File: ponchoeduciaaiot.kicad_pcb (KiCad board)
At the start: 2 copper layers, 41 parts, among them J1 TB_1X3, J2 TB_1X2, J3 TB_1X2, Q1 BC548, Q2 BC548, U1 4N25, U2 LM35, U3 4N25, U4 RELAY, U5 RELAY, U6 RN1810E

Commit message: placing de componentes
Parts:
- moved D8 224.7 mm to (38.8, 35.0), turned to 90 degrees
- moved C6 218.9 mm to (54.0, 31.0), turned to 90 degrees
- moved C2 215.9 mm to (52.0, 51.2), turned to 90 degrees
- moved C1 209.0 mm to (60.0, 32.5), turned to 90 degrees
- moved R15 206.5 mm to (38.8, 28.8)
- moved C4 197.5 mm to (58.0, 52.8), turned to 90 degrees
- moved R13 195.1 mm to (63.0, 60.0), turned to 90 degrees
- moved R12 177.6 mm to (68.0, 60.0), turned to 90 degrees
- moved R14 172.5 mm to (73.2, 52.8)
- moved C5 170.9 mm to (90.8, 32.2), turned to 90 degrees
- moved C3 159.8 mm to (96.8, 30.8), turned to 90 degrees
- moved U6 158.9 mm to (66.2, 47.0)
- moved U2 155.1 mm to (116.0, 33.5), turned to 90 degrees
- moved R7 118.2 mm to (109.8, 38.8), turned to 90 degrees
- moved D3 113.3 mm to (106.5, 44.0)
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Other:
- board outline added: 86.5 x 96.5 mm

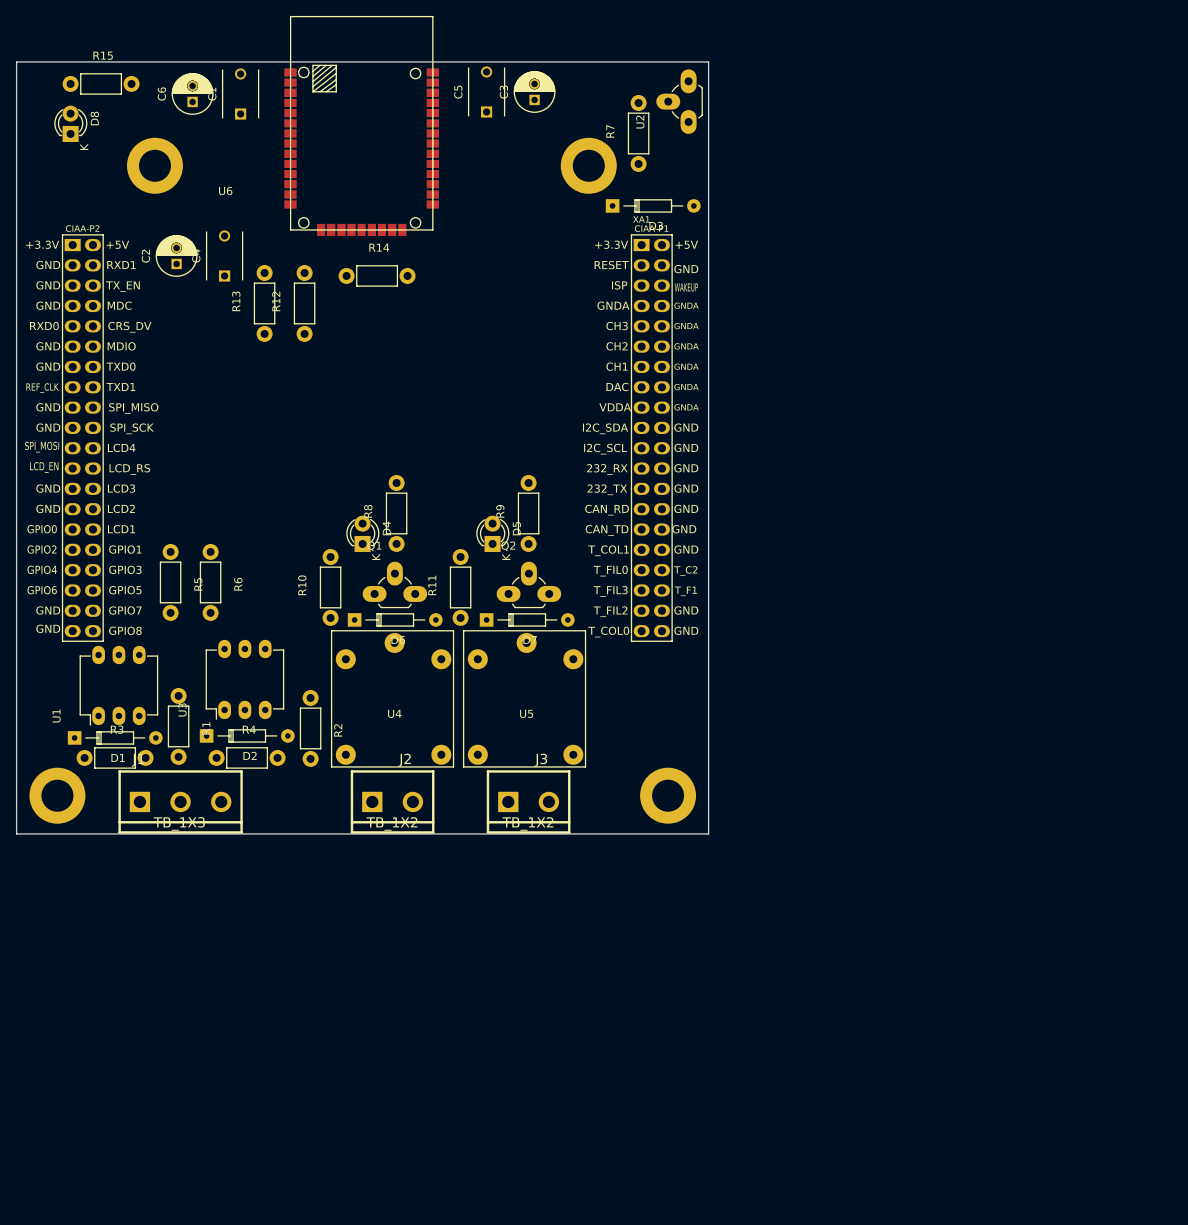
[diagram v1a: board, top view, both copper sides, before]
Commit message: correcciones en esquemarico. ERC OK. Se crearon rotulos. PCB: replacing mas compacto
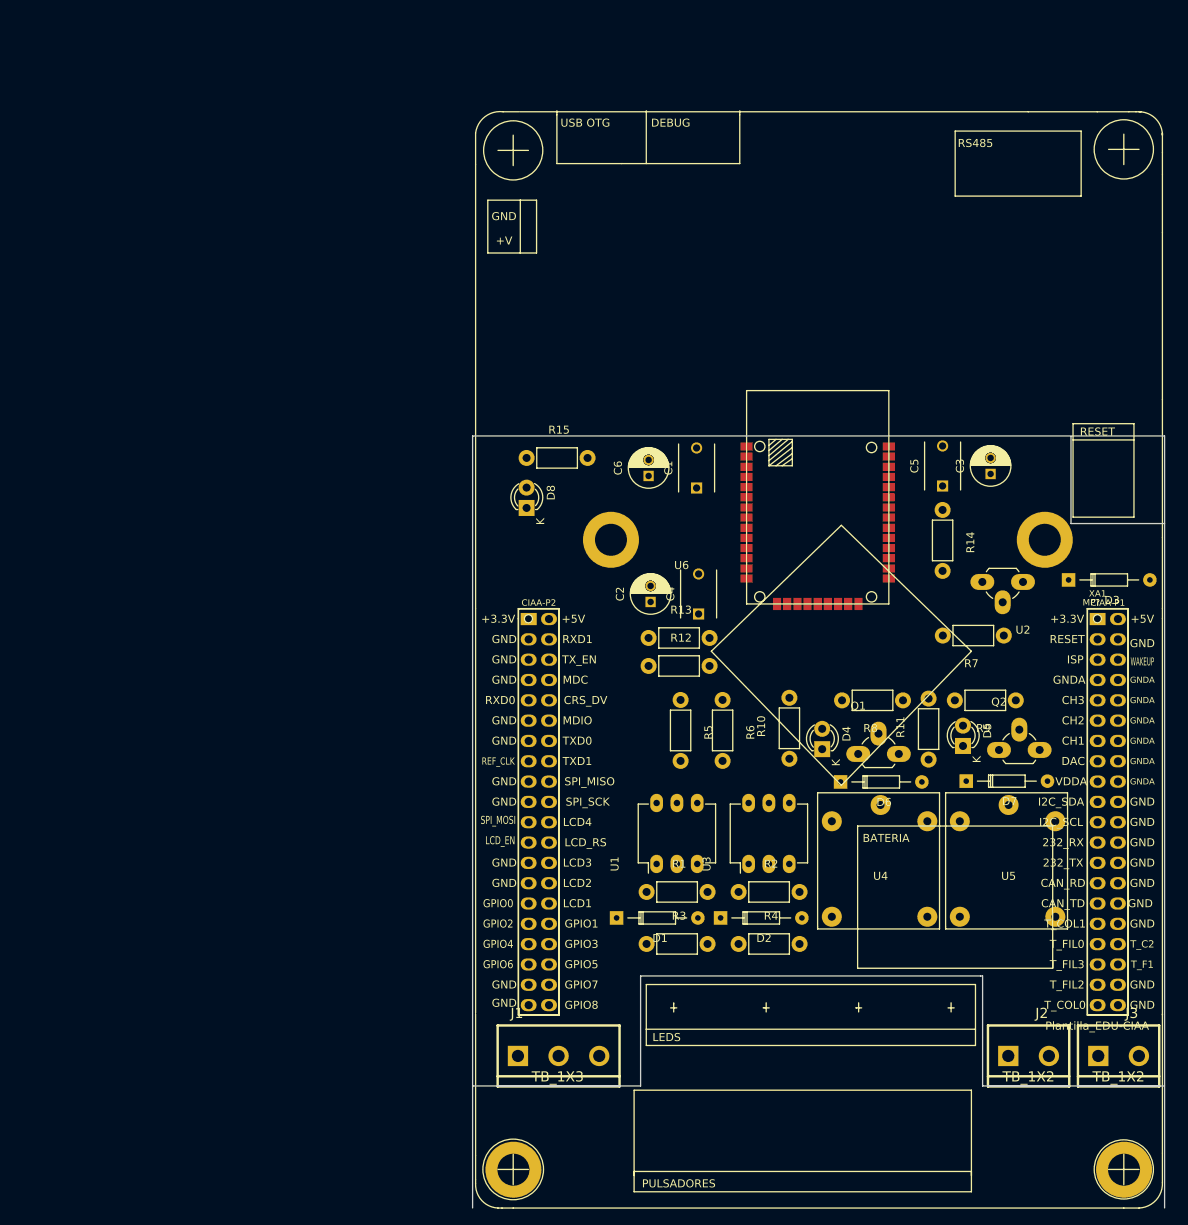
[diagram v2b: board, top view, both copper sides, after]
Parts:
- added MP?: Plantilla_EDU-CIAA, ponchoeduciaaiot:Plantilla_EDU-CIAA, F.Cu at (167.1, 95.6)
- moved J2 85.6 mm to (158.5, 150.2)
- moved J3 80.3 mm to (169.8, 150.2)
- moved R14 80.0 mm to (147.8, 82.0), turned to 270 degrees
- moved R7 74.6 mm to (155.4, 97.7), turned to 180 degrees
- moved R3 74.0 mm to (110.8, 136.2)
- moved C1 73.7 mm to (117.0, 79.2)
- moved C3 73.7 mm to (153.8, 77.5)
- moved C5 73.7 mm to (147.8, 79.0)
- moved C6 73.7 mm to (111.0, 77.8)
- moved D3 73.7 mm to (163.5, 90.8)
- moved D8 73.7 mm to (95.8, 81.8)
- moved R15 73.7 mm to (95.8, 75.5)
- moved U6 73.7 mm to (123.2, 93.8)
- moved XA1 73.7 mm to (167.1, 95.6)
- moved C2 72.8 mm to (111.2, 93.5)
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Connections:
- D2 pad 2: Net-(D2-Pad2) -> Net-(D1-Pad2)
- R4 pad 2: Net-(D2-Pad2) -> Net-(D1-Pad2)
- U3 pad 2: Net-(D2-Pad2) -> Net-(D1-Pad2)
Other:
- outline, holes or cut-outs redrawn
- board text added: "Extra information:"
- board text added: "Grid: 0.2500mm Track with:1mm Via:0.6mm / 0.4mm Layers: 2 PCB Surface Finishes: HASL"

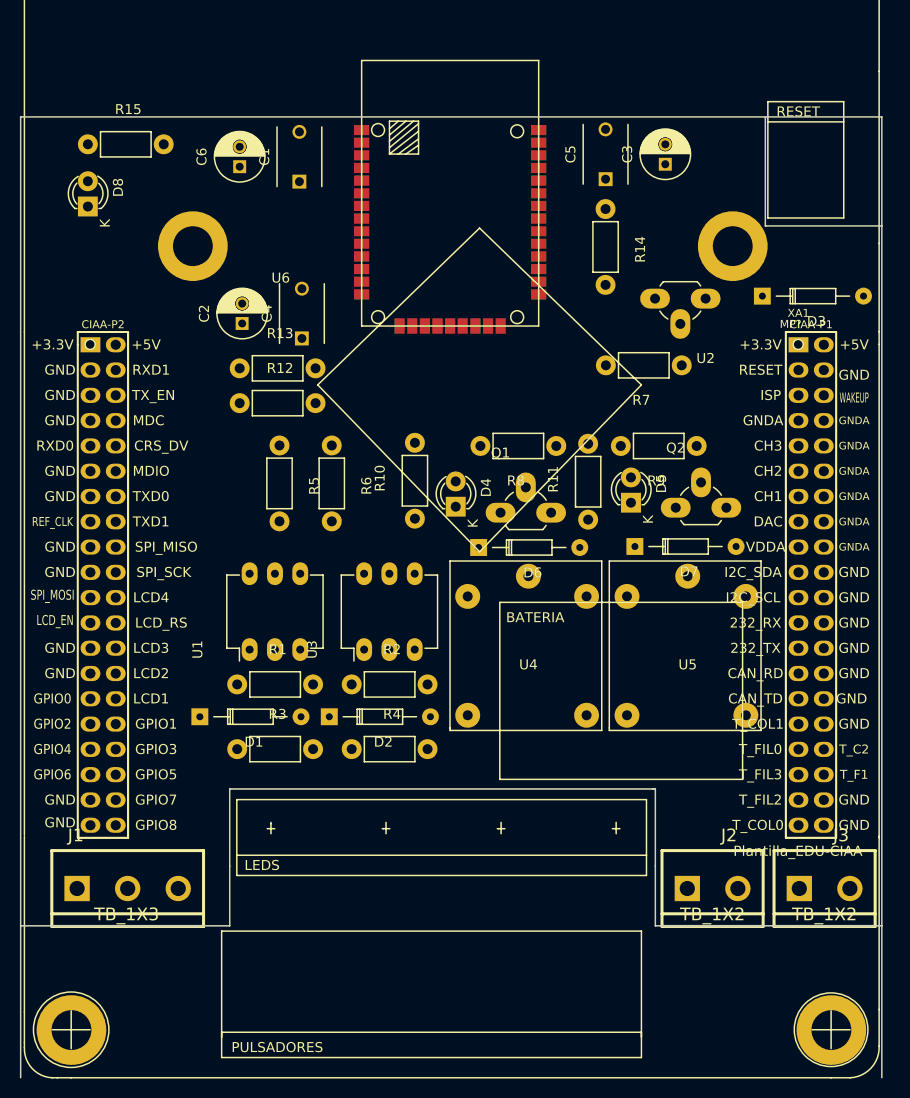
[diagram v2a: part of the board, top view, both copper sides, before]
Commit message: comienzo ruteo
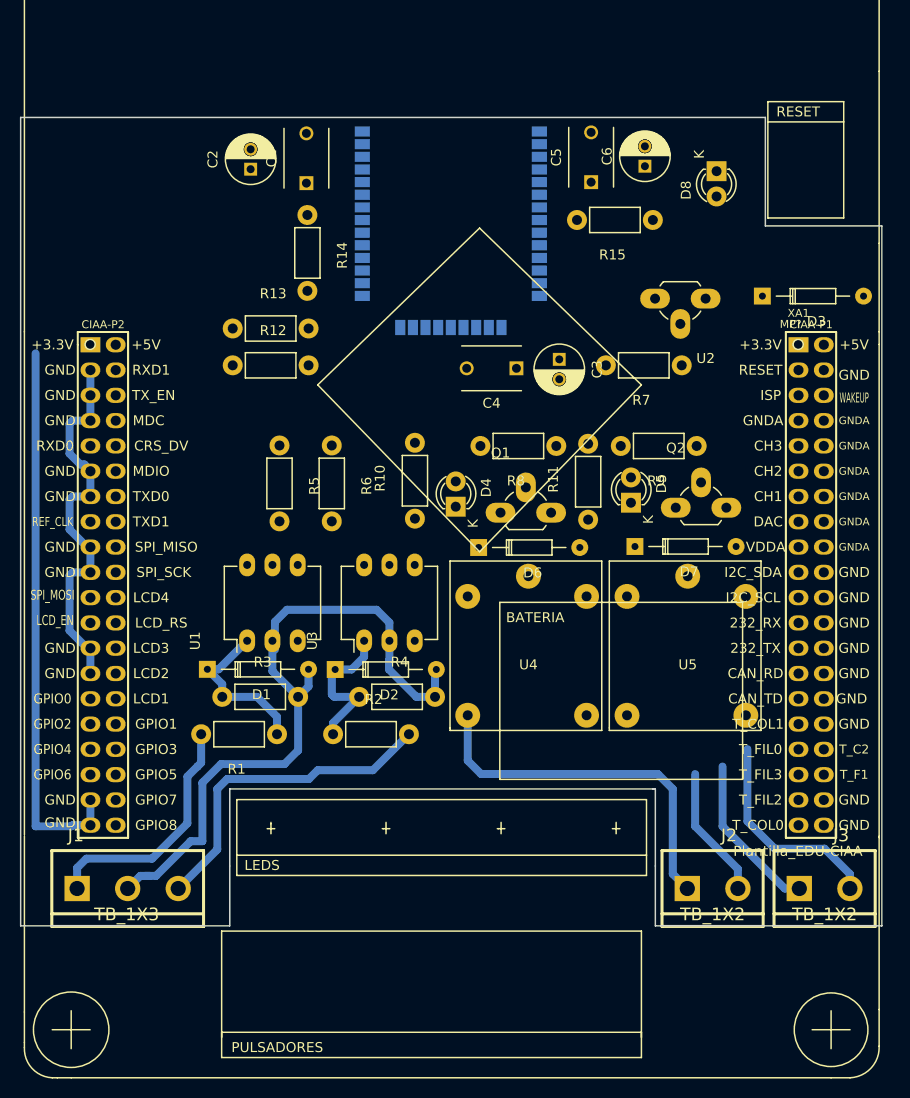
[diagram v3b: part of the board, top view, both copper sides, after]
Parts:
- U6: moved to B.Cu
- moved D8 63.2 mm to (158.9, 78.2), turned to 270 degrees
- moved R15 57.3 mm to (152.5, 83.1), turned to 180 degrees
- moved C6 40.7 mm to (151.7, 77.7)
- moved R14 30.0 mm to (117.8, 82.6)
- moved C3 22.3 mm to (143.1, 97.1), turned to 270 degrees
- moved C4 21.8 mm to (138.8, 98.0), turned to 180 degrees
- moved U6 17.9 mm to (141.1, 93.9), turned to 180 degrees
- moved C2 15.5 mm to (112.1, 78.0)
- moved R1 6.40 mm to (114.8, 134.8), turned to 180 degrees
- moved R3 5.46 mm to (109.2, 131.0)
- moved R2 5.34 mm to (120.4, 134.8)
- moved R4 5.30 mm to (123.0, 131.0)
- moved D1 4.82 mm to (107.8, 128.2)
- moved D2 4.78 mm to (120.6, 128.3)
- moved R13 4.06 mm to (110.3, 94.0)
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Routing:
- net GND: track 0.00 -> 95.1 mm
- net Net-(D1-Pad2): track 0.00 -> 71.6 mm
- net Net-(J2-Pad1): track 0.00 -> 36.9 mm
- net Net-(J1-Pad3): track 0.00 -> 33.2 mm
- net Net-(J1-Pad1): track 0.00 -> 24.5 mm
- net Net-(J3-Pad2): track 0.00 -> 21.2 mm
- net Net-(D1-Pad1): track 0.00 -> 16.6 mm
- net Net-(J3-Pad1): track 0.00 -> 16.3 mm
- net Net-(D2-Pad1): track 0.00 -> 15.4 mm
- net Net-(J2-Pad2): track 0.00 -> 13.3 mm
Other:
- board size 86.5 x 96.5 mm -> 86.5 x 81.2 mm
- net class Default: clearance 0.2 -> 0.7; trace_width 0.25 -> 0.8; via_dia 0.6 -> 1.27; via_drill 0.4 -> 0.8
- rule trace_clearance: 0.2 -> 0.7
- rule trace_min: 0.2 -> 0.8
- rule via_min_drill: 0.3 -> 0.8
- rule via_min_size: 0.4 -> 1.27
- board text added: "Grid: 0.2500mm Track with:0.8mm Via:0.6mm / 0.4mm Layers: 2 PCB Surface Finishes: HASL"
- board text removed: "Grid: 0.2500mm Track with:1mm Via:0.6mm / 0.4mm Layers: 2 PCB Surface Finishes: HASL"

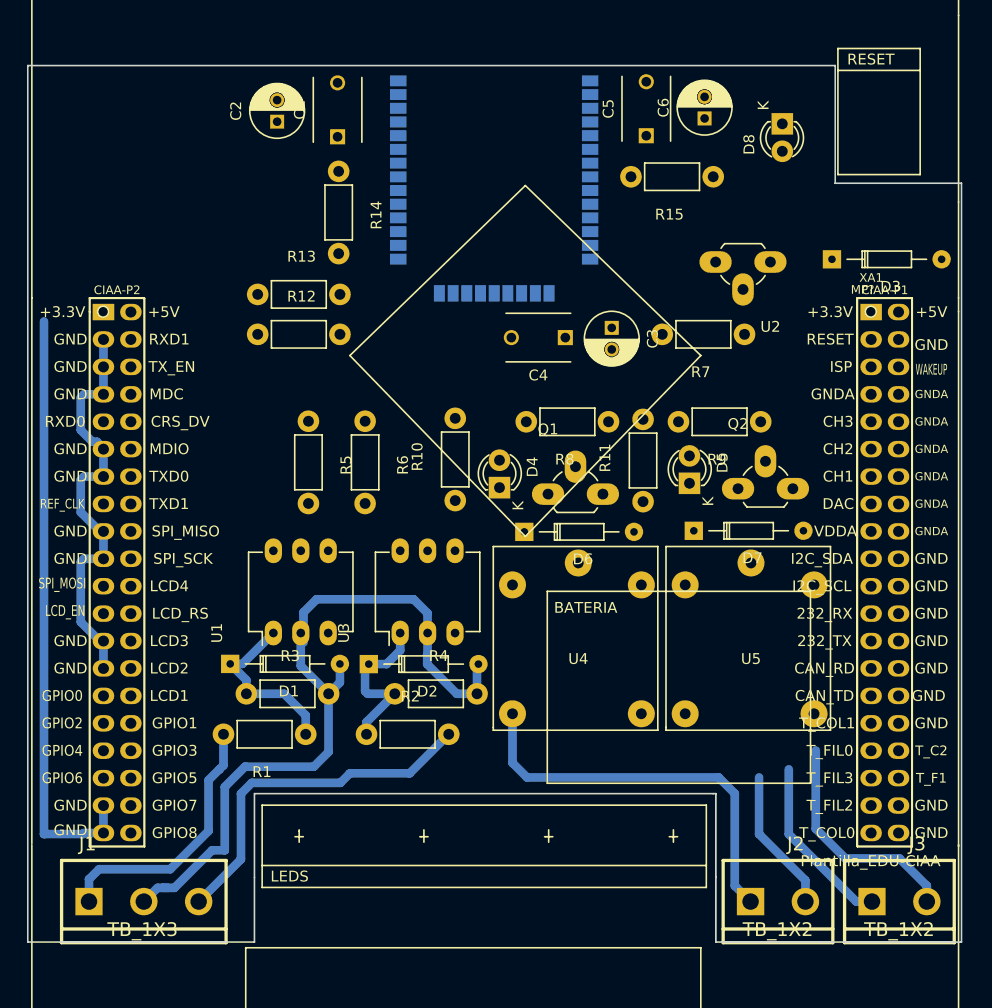
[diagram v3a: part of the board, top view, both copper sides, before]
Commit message: ruteo casi terminado. falta modulo wifi
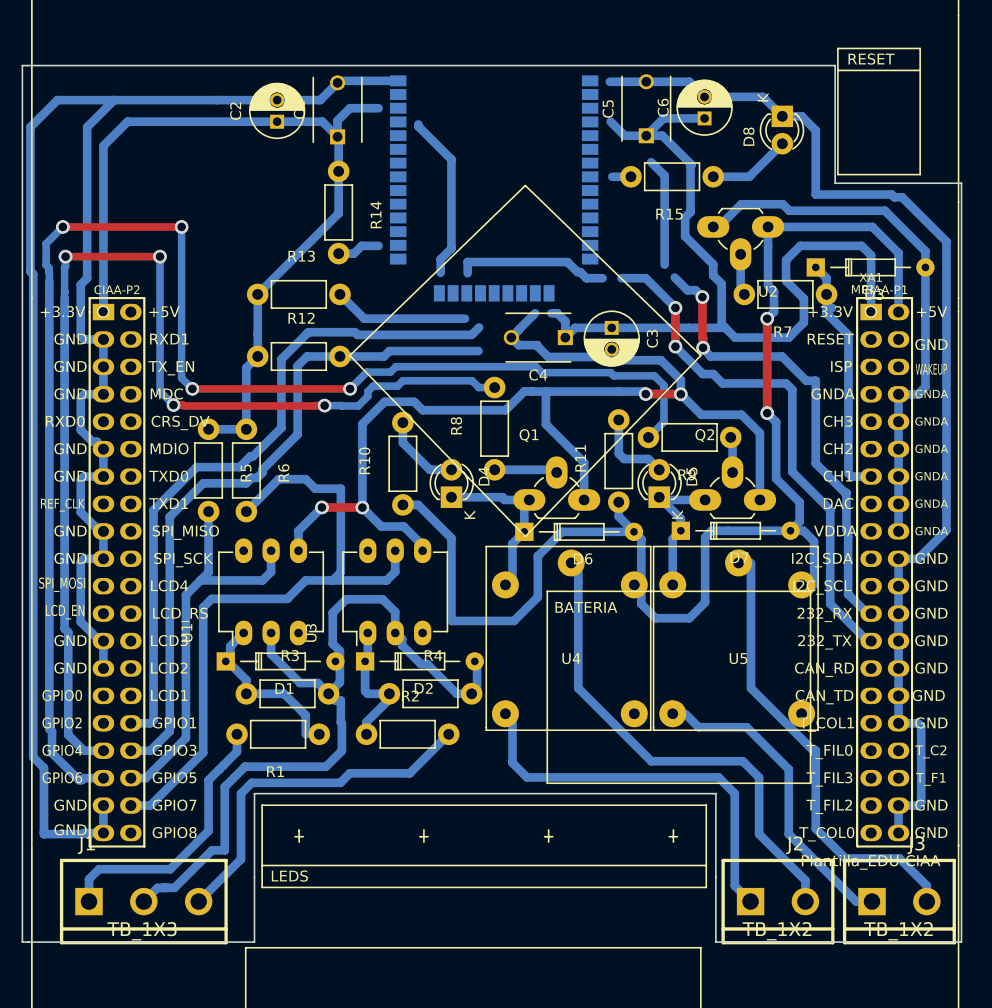
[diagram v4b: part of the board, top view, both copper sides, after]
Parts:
- moved R8 11.5 mm to (132.2, 110.2), turned to 90 degrees
- moved R6 11.0 mm to (109.2, 106.5)
- moved R5 9.28 mm to (105.8, 106.5)
- moved R7 8.45 mm to (163.0, 94.0)
- moved R10 4.87 mm to (123.8, 113.5)
- moved D4 4.54 mm to (128.2, 112.8)
- moved U2 3.26 mm to (157.6, 87.8)
- moved Q2 3.22 mm to (151.8, 113.0)
- moved R9 3.14 mm to (154.1, 107.2)
- moved D5 3.08 mm to (147.5, 112.8)
- moved U3 3.00 mm to (120.5, 125.4)
- moved U1 2.75 mm to (109.0, 125.4)
- moved R11 2.25 mm to (143.8, 113.2)
- moved R12 2.05 mm to (110.3, 99.8)
- moved Q1 1.82 mm to (135.5, 113.0)
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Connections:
- XA1 pad 4: GND -> Net-(XA1-Pad4)
- XA1 pad 42: +5V -> Net-(XA1-Pad42)
- XA1 pad 69: /gpios/IN0 -> Net-(XA1-Pad69)
- XA1 pad 71: /gpios/IN1 -> Net-(XA1-Pad71)
- XA1 pad 72: /ConectoresPoncho/MODULE_RESET -> /comm/CMD_CTRL
- XA1 pad 74: /comm/CMD_CTRL -> /ConectoresPoncho/MODULE_RESET
- XA1 pad 76: Net-(XA1-Pad76) -> /gpios/IN0
- XA1 pad 78: Net-(XA1-Pad78) -> /gpios/IN1
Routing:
- net GND: track 95.1 -> 381.8 mm, vias 0 -> 4
- net +3V3: track 0.00 -> 159.3 mm
- net /gpios/OUT1: track 0.00 -> 132.6 mm, vias 0 -> 4
- net +5V: track 0.00 -> 123.0 mm, vias 0 -> 2
- net /gpios/OUT0: track 0.00 -> 103.0 mm, vias 0 -> 4
- net /comm/CMD_CTRL: track 0.00 -> 63.4 mm
- net /ConectoresPoncho/MODULE_RESET: track 0.00 -> 63.1 mm
- net /gpios/IN1: track 0.00 -> 62.5 mm
- net /ConectoresPoncho/TXD_EDUCIAA: track 0.00 -> 61.4 mm, vias 0 -> 2
- net GNDA: track 0.00 -> 50.4 mm
- net /ConectoresPoncho/RXD_EDUCIAA: track 0.00 -> 43.7 mm, vias 0 -> 2
- net (no net): track 0.00 -> 39.6 mm
- net /gpios/IN0: track 0.00 -> 37.3 mm
- net Net-(J2-Pad2): track 13.3 -> 45.1 mm
- net /ConectoresPoncho/ANALOG_IN: track 0.00 -> 23.3 mm
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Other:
- board size 86.5 x 81.2 mm -> 87 x 81.2 mm
- net class MODULE NETS added: clearance 0.3, trace_width 0.5, via_dia 1.27, via_drill 0.8
- net class OUTS BUS added: clearance 0.6, trace_width 0.7, via_dia 1.27, via_drill 0.8
- rule trace_min: 0.8 -> 0.5
- board text added: "Grid: 0.2500mm Track with:0.8mm Via:1.27mm / 0.8mm Layers: 1 PCB Surface Finishes: HASL"
- board text removed: "Grid: 0.2500mm Track with:0.8mm Via:0.6mm / 0.4mm Layers: 2 PCB Surface Finishes: HASL"
